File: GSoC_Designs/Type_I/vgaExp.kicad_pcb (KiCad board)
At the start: 2 copper layers, 80 x 60.1 mm, 70 parts, among them J1 DE-15, J2 DE-15, J3 VHDCI, P1 50R, P2 50R, P3 50R, P4 50R, P5 CONN_1, P6 CONN_1, U1 ADP3303-3V3, U2 ADP3334, U3 AD9984, U4 ADP3334

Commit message: PCB Routing
70% tracks routed. Fine tuning remaining
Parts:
- removed C10, C13, C7: 47nf, SM0805
- removed C11: 1nf, SM0805
- removed FB1, FB2, FB3: FILTER, SM0805
- removed P1, P2, P3, P4: 50R, R50x8
- removed R19, R20, R21, R22: 50R, SM0805
- added P7: CONN_6, PIN_ARRAY-6X1, F.Cu at (148.0, 92.5)
- added R23: 2.2K, SM0805, F.Cu at (128.6, 107.3)
- added R24: 4.7K, SM0805, F.Cu at (126.9, 102.8)
- added R25: 4.7K, SM0805, F.Cu at (142.1, 55.8)
- added R26: 4.7K, SM0805, F.Cu at (142.2, 53.7)
- added R27: 4.7K, SM0805, F.Cu at (126.9, 99.9)
- added TP1: TESTPOINT, PIN_ARRAY_1, F.Cu at (153.0, 64.4)
- added TP10: TESTPOINT, PIN_ARRAY_1, F.Cu at (133.4, 51.2)
- added TP11: TESTPOINT, PIN_ARRAY_1, F.Cu at (130.9, 97.5)
- added TP12: TESTPOINT, PIN_ARRAY_1, F.Cu at (95.2, 52.0)
- added TP13: TESTPOINT, PIN_ARRAY_1, F.Cu at (96.6, 60.7)
- added TP2: TESTPOINT, PIN_ARRAY_1, F.Cu at (153.0, 67.0)
- added TP3: TESTPOINT, PIN_ARRAY_1, F.Cu at (126.8, 67.8)
- added TP4: TESTPOINT, PIN_ARRAY_1, F.Cu at (134.7, 67.7)
- added TP5: TESTPOINT, PIN_ARRAY_1, F.Cu at (132.1, 67.7)
- added TP6: TESTPOINT, PIN_ARRAY_1, F.Cu at (129.5, 67.8)
- added TP7: TESTPOINT, PIN_ARRAY_1, F.Cu at (107.3, 91.3)
- added TP8: TESTPOINT, PIN_ARRAY_1, F.Cu at (104.7, 91.3)
- added TP9: TESTPOINT, PIN_ARRAY_1, F.Cu at (115.3, 52.0)
- added U5: 24AA014, -SOIC8, F.Cu at (107.3, 97.1)
- added U6: TCA9617A, SSOP8, F.Cu at (142.6, 60.4)
- added U7: TCA9617A, SSOP8, F.Cu at (130.9, 103.0)
- C17, C18, C19, C2, C21, C22, C23, C24, C25, C3, C4, C5: footprint SM0603 -> SM0805
- Cp1: footprint -PANASONIC_D -> -PANASONIC_D_CorrectedPadNumbers
- Cp2, Cp3, Cp5, Cp6: footprint -PANASONIC_E -> -PANASONIC_E_CorrectedPad
- Cp4: footprint -PANASONIC_C -> -PANASONIC_C_correctedPad
- FB4, FB5, FB6: moved to F.Cu
- R1, R3, R5: value 75R -> 2.2K
- moved R3 29.5 mm to (133.3, 107.4)
- moved R5 19.1 mm to (141.2, 64.9)
- moved R14 7.52 mm to (121.7, 107.7)
- moved R1 6.96 mm to (142.8, 67.3)
- turned FB6 to 180 degrees
- turned FB5 to 180 degrees
- turned FB4 to 180 degrees
- turned C12 to 180 degrees
- turned C6 to 180 degrees
- turned C8 to 180 degrees
- turned C9 to 180 degrees
- turned Cp6 to 90 degrees
- turned R13 to 270 degrees
- turned R18 to 0 degrees
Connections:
- C15 pad 1: /PVD -> /PowerSupply/PVD
- C15 pad 2: N-00000138 -> N-000001
- C16 pad 1: /PVD -> /PowerSupply/PVD
- C16 pad 2: N-000001 -> N-000005
- C17 pad 2: /PowerSupply/GND -> /I2C/DDC Section/GND
- C18 pad 2: /PowerSupply/GND -> /I2C/DDC Section/GND
- C19 pad 2: /PowerSupply/GND -> /I2C/DDC Section/GND
- C2 pad 1: /PowerSupply/OVDD -> /I2C/DDC Section/OVDD
- C2 pad 2: /PowerSupply/GND -> /I2C/DDC Section/GND
- C21 pad 2: /PowerSupply/GND -> /I2C/DDC Section/GND
- C22 pad 2: /PowerSupply/GND -> /I2C/DDC Section/GND
- C23 pad 2: /PowerSupply/GND -> /I2C/DDC Section/GND
- C24 pad 2: /PowerSupply/GND -> /I2C/DDC Section/GND
- C25 pad 2: /PowerSupply/GND -> /I2C/DDC Section/GND
- C3 pad 1: /PowerSupply/OVDD -> /I2C/DDC Section/OVDD
- C3 pad 2: /PowerSupply/GND -> /I2C/DDC Section/GND
- C4 pad 1: /PowerSupply/OVDD -> /I2C/DDC Section/OVDD
- C4 pad 2: /PowerSupply/GND -> /I2C/DDC Section/GND
- C5 pad 1: /PowerSupply/OVDD -> /I2C/DDC Section/OVDD
- C5 pad 2: /PowerSupply/GND -> /I2C/DDC Section/GND
- FB4 pad 1: N-0000037 -> /B
- FB5 pad 1: N-0000068 -> /G
- FB6 pad 1: N-0000072 -> /R
- J1 pad 1: N-0000071 -> /R
- J1 pad 10: (no net) -> /I2C/DDC Section/GND
- J1 pad 12: (no net) -> /I2C/DDC Section/SDA_VGA_TX
- J1 pad 13: (no net) -> /HSYNC0
- J1 pad 14: (no net) -> /VSYNC0
- J1 pad 15: (no net) -> /I2C/DDC Section/SCL_VGA_TX
- J1 pad 2: N-0000070 -> /G
- J1 pad 3: N-0000069 -> /B
- J1 pad 4: /GND -> (no net)
- J1 pad 5: /GND -> /I2C/DDC Section/GND
- J1 pad 6: /GND -> /I2C/DDC Section/GND
- J1 pad 7: /GND -> /I2C/DDC Section/GND
- J1 pad 8: /GND -> /I2C/DDC Section/GND
- J1 pad 9: /GND -> (no net)
- J2 pad 1: N-0000072 -> /R
- J2 pad 10: (no net) -> /I2C/DDC Section/GND
- J2 pad 12: (no net) -> /I2C/DDC Section/SDA_VGA_RX
- J2 pad 13: (no net) -> /HSYNC0
- J2 pad 14: (no net) -> /VSYNC0
- J2 pad 15: (no net) -> /I2C/DDC Section/SCL_VGA_RX
- J2 pad 2: N-0000068 -> /G
- J2 pad 3: N-0000037 -> /B
- J2 pad 4: /GND -> (no net)
- J2 pad 5: /GND -> /I2C/DDC Section/GND
- J2 pad 6: /GND -> /I2C/DDC Section/GND
- J2 pad 7: /GND -> /I2C/DDC Section/GND
- J2 pad 8: /GND -> /I2C/DDC Section/GND
- J2 pad 9: /GND -> (no net)
- J3 pad 11: /GND -> /I2C/DDC Section/GND
- J3 pad 14: /GND -> /I2C/DDC Section/GND
- J3 pad 17: /VCC -> /I2C/DDC Section/VCC
- J3 pad 18: /VCC -> /I2C/DDC Section/VCC
- J3 pad 2: /GND -> /I2C/DDC Section/GND
- J3 pad 21: /GND -> /I2C/DDC Section/GND
- J3 pad 24: /GND -> /I2C/DDC Section/GND
- J3 pad 27: /GND -> /I2C/DDC Section/GND
- J3 pad 30: /GND -> /I2C/DDC Section/GND
- J3 pad 33: /GND -> /I2C/DDC Section/GND
- J3 pad 34: (no net) -> /I2C/DDC Section/SDA_INT
- J3 pad 35: /OE_Field -> /I2C/DDC Section/SCL_VGA_RX_BUF
- J3 pad 36: N-0000067 -> /I2C/DDC Section/GND
- J3 pad 37: /PWRDWN -> /I2C/DDC Section/SDA_VGA_RX_BUF
- J3 pad 39: N-0000067 -> /I2C/DDC Section/GND
- J3 pad 42: N-0000067 -> /I2C/DDC Section/GND
- J3 pad 45: N-0000067 -> /I2C/DDC Section/GND
- J3 pad 48: N-0000067 -> /I2C/DDC Section/GND
- J3 pad 5: /GND -> /I2C/DDC Section/GND
- J3 pad 51: /VCC -> /I2C/DDC Section/VCC
- J3 pad 52: /VCC -> /I2C/DDC Section/VCC
- J3 pad 55: N-0000067 -> /I2C/DDC Section/GND
- J3 pad 58: N-0000067 -> /I2C/DDC Section/GND
- J3 pad 61: N-0000067 -> /I2C/DDC Section/GND
- J3 pad 64: N-0000067 -> /I2C/DDC Section/GND
- J3 pad 65: /CLAMP -> /I2C/DDC Section/SCL_VGA_TX_BUF
- J3 pad 66: /COST -> /I2C/DDC Section/SDA_VGA_TX_BUF
- J3 pad 67: N-0000067 -> /I2C/DDC Section/GND
- J3 pad 68: (no net) -> /I2C/DDC Section/SCL_INT
- J3 pad 8: /GND -> /I2C/DDC Section/GND
- P5 pad 1: (no net) -> /I2C/DDC Section/GND
- P6 pad 1: (no net) -> /I2C/DDC Section/VCC
- R1 pad 1: N-0000078 -> /I2C/DDC Section/OVDD
- R1 pad 2: N-0000054 -> /I2C/DDC Section/SDA_VGA_RX_BUF
- R10 pad 1: (no net) -> /I2C/DDC Section/GND
- R11 pad 1: /GND -> /I2C/DDC Section/GND
- R12 pad 1: /GND -> /I2C/DDC Section/GND
- R14 pad 1: /PowerSupply/GND -> /I2C/DDC Section/GND
- R15 pad 1: N-000005 -> /I2C/DDC Section/SCL_INT
- R15 pad 2: /OVDD -> /I2C/DDC Section/OVDD
- R16 pad 1: N-000006 (its old number) -> /I2C/DDC Section/SDA_INT
- R16 pad 2: /OVDD -> /I2C/DDC Section/OVDD
- R18 pad 1: /PowerSupply/GND -> /I2C/DDC Section/GND
- R2 pad 2: N-0000077 -> /I2C/DDC Section/GND
- R3 pad 1: N-0000078 -> /I2C/DDC Section/OVDD
- R3 pad 2: N-0000056 -> /I2C/DDC Section/SDA_VGA_TX_BUF
- R4 pad 2: N-0000077 -> /I2C/DDC Section/GND
- R5 pad 1: N-0000078 -> /I2C/DDC Section/OVDD
- R5 pad 2: N-0000055 -> /I2C/DDC Section/SCL_VGA_RX_BUF
- R6 pad 2: N-0000077 -> /I2C/DDC Section/GND
- R7 pad 1: (no net) -> /I2C/DDC Section/GND
- R8 pad 1: N-00000138 -> N-000005
- R9 pad 1: (no net) -> /I2C/DDC Section/OVDD
- U1 pad 1: /PowerSupply/OVDD -> /I2C/DDC Section/OVDD
- U1 pad 2: /PowerSupply/OVDD -> /I2C/DDC Section/OVDD
- U1 pad 4: /PowerSupply/GND -> /I2C/DDC Section/GND
- U1 pad 5: /PowerSupply/VCC -> /I2C/DDC Section/VCC
- U1 pad 7: /PowerSupply/VCC -> /I2C/DDC Section/VCC
- U1 pad 8: /PowerSupply/VCC -> /I2C/DDC Section/VCC
- U2 pad 1: /PowerSupply/GND -> /I2C/DDC Section/GND
- U2 pad 2: /PowerSupply/GND -> /I2C/DDC Section/GND
- U2 pad 3: /PowerSupply/VCC -> /I2C/DDC Section/VCC
- U2 pad 4: /PowerSupply/VCC -> /I2C/DDC Section/VCC
- U3 pad 1: /VD -> /PowerSupply/VD
- U3 pad 10: N-0000082 -> (no net)
- U3 pad 11: /GND -> /I2C/DDC Section/GND
- U3 pad 12: N-0000083 -> (no net)
- U3 pad 13: /VD -> /PowerSupply/VD
- U3 pad 15: /GND -> /I2C/DDC Section/GND
- U3 pad 16: N-0000085 (its old number) -> (no net)
- U3 pad 21: N-000007 (its old number) -> /OE_Field
- U3 pad 22: N-0000010 (its old number) -> /VSOUT
- U3 pad 23: N-000009 (its old number) -> /HSOUT
- U3 pad 24: N-000008 (its old number) -> /SOGOUT
- U3 pad 25: N-0000033 -> /DATACK
- U3 pad 26: (no net) -> /I2C/DDC Section/OVDD
- U3 pad 27: (no net) -> /I2C/DDC Section/GND
- U3 pad 28: N-0000032 -> /R9
- U3 pad 29: N-0000031 -> /R8
- U3 pad 3: /GND -> /I2C/DDC Section/GND
- U3 pad 30: N-0000030 -> /R7
- U3 pad 31: N-0000029 -> /R6
- U3 pad 32: N-0000028 -> /R5
- U3 pad 33: N-0000027 -> /R4
- U3 pad 34: N-0000026 -> /R3
- U3 pad 35: N-0000025 -> /R2
- U3 pad 36: N-0000015 -> /R1
- U3 pad 37: N-0000024 -> /R0
- U3 pad 38: (no net) -> /I2C/DDC Section/OVDD
- U3 pad 39: N-0000076 -> /I2C/DDC Section/GND
- U3 pad 4: N-0000079 -> (no net)
- U3 pad 40: N-0000076 -> /I2C/DDC Section/GND
- U3 pad 41: /VD -> /PowerSupply/VD
- U3 pad 42: N-00000111 -> /G9
- U3 pad 43: N-00000112 -> /G8
- U3 pad 44: N-00000113 -> /G7
- U3 pad 45: N-00000131 -> /G6
- U3 pad 46: N-00000130 -> /G5
- U3 pad 47: N-00000134 -> /G4
- U3 pad 48: N-00000119 -> /G3
- U3 pad 49: N-00000122 -> /G2
- U3 pad 5: /VD -> /PowerSupply/VD
- U3 pad 50: N-00000115 -> /G1
- U3 pad 51: N-00000117 -> /G0
- U3 pad 52: (no net) -> /I2C/DDC Section/OVDD
- U3 pad 53: (no net) -> /I2C/DDC Section/GND
- U3 pad 54: N-00000114 -> /B9
- U3 pad 55: N-00000132 -> /B8
- U3 pad 56: N-00000133 -> /B7
- U3 pad 57: N-00000135 -> /B6
- U3 pad 58: N-00000120 -> /B5
- U3 pad 59: N-00000118 -> /B4
- U3 pad 60: N-00000116 -> /B3
- U3 pad 61: N-000003 -> /B2
- U3 pad 62: N-000002 -> /B1
- U3 pad 63: N-000004 -> /B0
- U3 pad 64: (no net) -> /I2C/DDC Section/OVDD
- U3 pad 65: (no net) -> /I2C/DDC Section/GND
- U3 pad 66: N-000006 (its old number) -> /I2C/DDC Section/SDA_INT
- U3 pad 67: N-000005 -> /I2C/DDC Section/SCL_INT
- U3 pad 68: (no net) -> /I2C/DDC Section/GND
- U3 pad 69: (no net) -> /I2C/DDC Section/GND
- U3 pad 7: /GND -> /I2C/DDC Section/GND
- U3 pad 70: (no net) -> /HSYNC0
- U3 pad 71: (no net) -> /VSYNC0
- U3 pad 74: /PVD -> /PowerSupply/PVD
- U3 pad 75: /GND -> /I2C/DDC Section/GND
- U3 pad 76: /PVD -> /PowerSupply/PVD
- U3 pad 77: /GND -> /I2C/DDC Section/GND
- U3 pad 78: N-00000138 -> N-000001
- U3 pad 79: /PVD -> /PowerSupply/PVD
- U3 pad 80: /GND -> /I2C/DDC Section/GND
- U3 pad 9: /VD -> /PowerSupply/VD
- U4 pad 1: /PowerSupply/GND -> /I2C/DDC Section/GND
- U4 pad 2: /PowerSupply/GND -> /I2C/DDC Section/GND
- U4 pad 3: /PowerSupply/VCC -> /I2C/DDC Section/VCC
- U4 pad 4: /PowerSupply/VCC -> /I2C/DDC Section/VCC
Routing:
- net /I2C/DDC Section/VCC: track 0.00 -> 132.5 mm, vias 0 -> 1
- net /HSYNC0: track 0.00 -> 80.2 mm
- net /VSYNC0: track 0.00 -> 77.3 mm
- net /I2C/DDC Section/SDA_VGA_RX_BUF: track 0.00 -> 65.9 mm
- net /I2C/DDC Section/SCL_VGA_RX_BUF: track 0.00 -> 63.7 mm
- net /I2C/DDC Section/SDA_VGA_TX_BUF: track 0.00 -> 56.7 mm, vias 0 -> 1
- net /I2C/DDC Section/SCL_VGA_TX_BUF: track 0.00 -> 51.2 mm, vias 0 -> 1
- net /B: track 0.00 -> 47.9 mm
- net /I2C/DDC Section/OVDD: track 0.00 -> 46.5 mm
- net /VSOUT: track 0.00 -> 44.3 mm, vias 0 -> 1
- net /G: track 0.00 -> 40.3 mm
- net /R: track 0.00 -> 37.1 mm
- net /HSOUT: track 0.00 -> 36.8 mm
- net /DATACK: track 0.00 -> 36.7 mm, vias 0 -> 1
- net /R9: track 0.00 -> 35.6 mm
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- added copper zone on B.Cu, net /I2C/DDC Section/GND
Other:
- net class Default: clearance 0.254 -> 0.125; trace_width 0.254 -> 0.125; via_dia 0.889 -> 0.45; via_drill 0.635 -> 0.3
- rule trace_clearance: 0.254 -> 0.125
- rule trace_min: 0.254 -> 0.125
- rule via_min_drill: 0.508 -> 0.3
- rule via_min_size: 0.889 -> 0.45

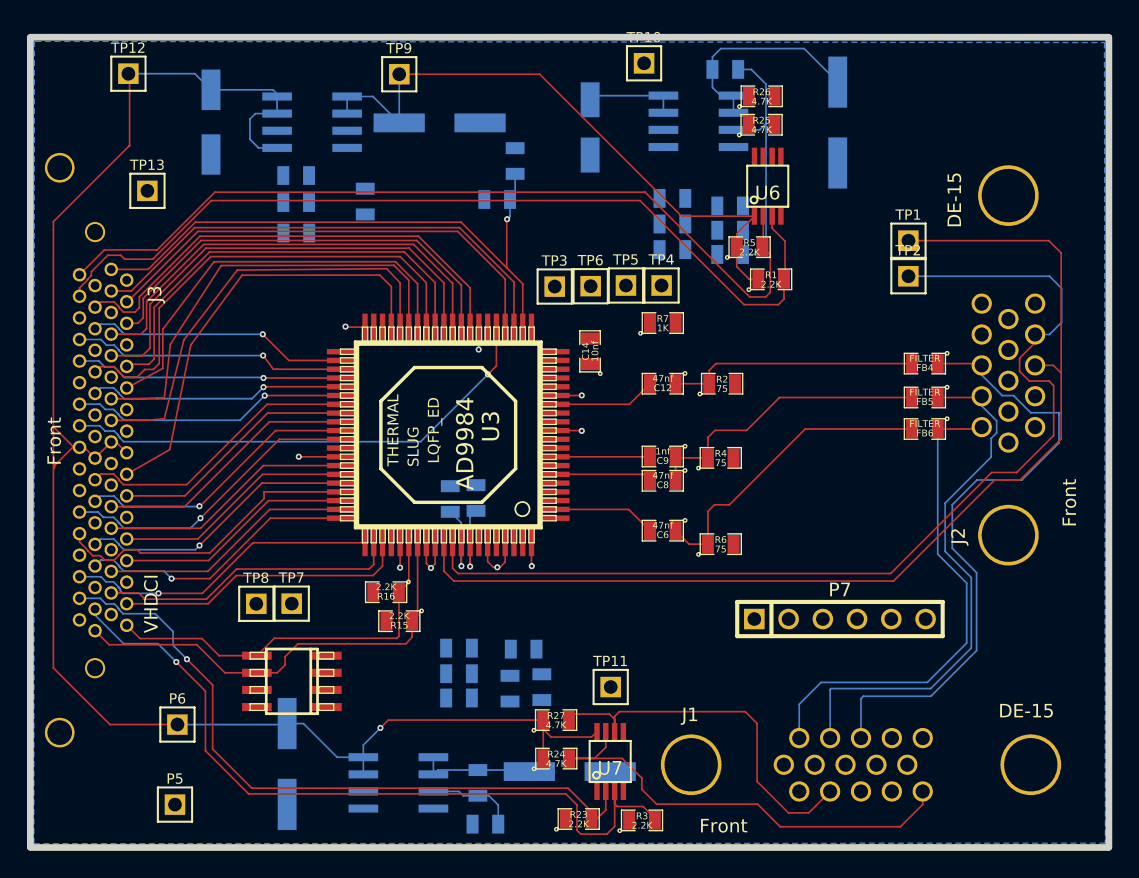
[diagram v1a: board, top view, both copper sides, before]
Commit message: All tracks routed. Optimizations and dine tuning remain
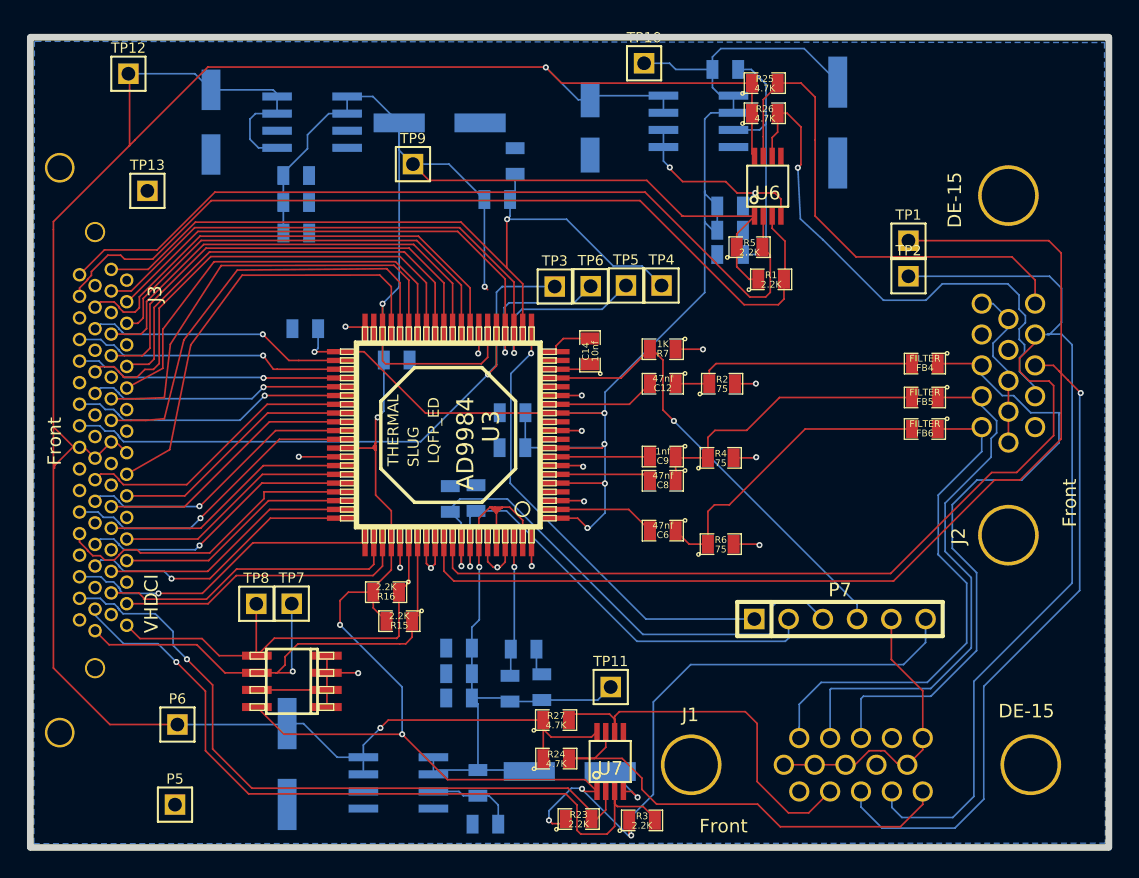
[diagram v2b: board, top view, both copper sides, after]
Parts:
- moved C21 27.9 mm to (108.3, 70.9)
- moved C22 20.4 mm to (123.7, 79.7)
- moved C23 19.8 mm to (123.7, 77.2)
- moved C5 12.0 mm to (115.1, 73.2), turned to 0 degrees
- moved TP9 6.74 mm to (116.3, 58.7)
- moved R25 3.10 mm to (142.4, 52.7)
- moved R7 1.94 mm to (134.8, 72.4), turned to 180 degrees
- moved R26 1.28 mm to (142.4, 54.9)
- turned R8 to 180 degrees
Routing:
- net /I2C/DDC Section/OVDD: track 46.5 -> 215.0 mm, vias 0 -> 8
- net /PowerSupply/VD: track 15.9 -> 111.9 mm, vias 0 -> 5
- net /I2C/DDC Section/GND: track 22.8 -> 99.7 mm, vias 9 -> 19
- net /I2C/DDC Section/VCC: track 132.5 -> 191.4 mm, vias 1 -> 2
- net /HSYNC0: track 80.2 -> 127.4 mm, vias 0 -> 1
- net /VSYNC0: track 77.3 -> 124.2 mm
- net /PowerSupply/PVD: track 8.56 -> 49.4 mm, vias 0 -> 1
- net /I2C/DDC Section/SDA_VGA_RX: track 0.00 -> 40.6 mm, vias 0 -> 1
- net /I2C/DDC Section/SCL_VGA_RX: track 0.00 -> 37.9 mm
- net /COST: track 6.10 -> 41.1 mm
- net /OE_Field: track 0.00 -> 34.6 mm, vias 0 -> 1
- net /PWRDWN: track 0.00 -> 34.3 mm, vias 0 -> 1
- net /CLAMP: track 6.07 -> 34.8 mm
- net /HSOUT: track 36.8 -> 50.7 mm, vias 0 -> 1
- net /VSOUT: track 44.3 -> 57.8 mm
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
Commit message: All Tracks routed. Tweaks. Ready for review
All Tracks routed. Tweaks. Ready for review. Some minor changes and
tweaks may be done before sending for Fab
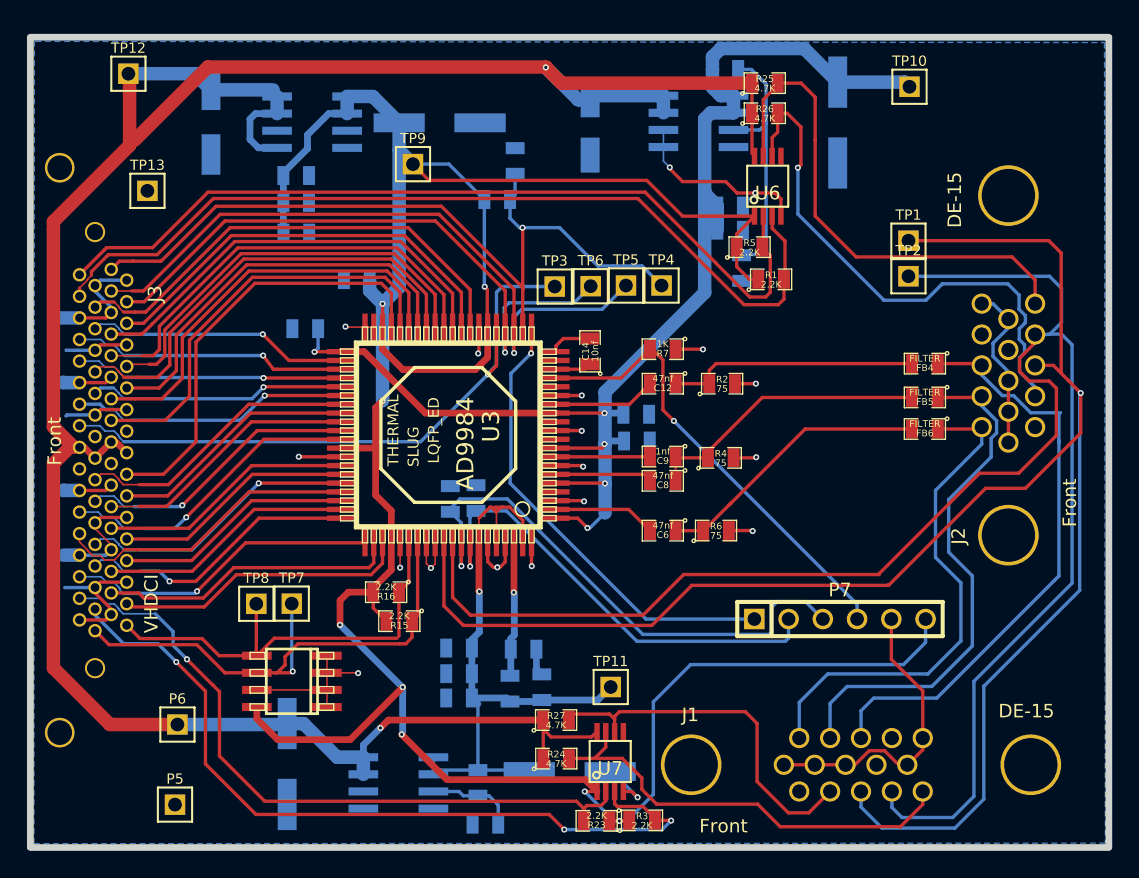
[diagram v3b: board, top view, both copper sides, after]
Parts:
- added ?: , OSHW-logo_silkscreen-back_10mm, B.Cu at (140.4, 83.0)
- moved TP10 19.8 mm to (153.1, 53.0)
- moved C22 9.25 mm to (132.9, 79.2), turned to 0 degrees
- moved C23 9.17 mm to (132.8, 77.3), turned to 0 degrees
- moved C5 6.65 mm to (112.1, 67.3), turned to 180 degrees
- moved R23 1.34 mm to (129.9, 107.4), turned to 180 degrees
- moved R18 1.32 mm to (140.7, 66.4), turned to 90 degrees
- moved R6 1.07 mm to (138.8, 85.9)
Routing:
- net /I2C/DDC Section/GND: track 99.7 -> 144.2 mm
- net /PowerSupply/VD: track 111.9 -> 100.5 mm
- net /VSYNC0: track 124.2 -> 128.3 mm
- net /HSYNC0: track 127.4 -> 131.4 mm
- net /B: track 47.9 -> 44.4 mm
- net /I2C/DDC Section/VCC: track 191.4 -> 188.5 mm
- net /I2C/DDC Section/SDA_VGA_TX_BUF: track 56.7 -> 58.9 mm, vias 1 -> 3
- net /B9: track 18.9 -> 21.1 mm
- net N-0000061: track 22.9 -> 21.0 mm
- net /R2: track 32.7 -> 31.0 mm
- net /R5: track 32.9 -> 31.1 mm
- net /R4: track 35.3 -> 33.7 mm
- net /VSOUT: track 57.8 -> 59.3 mm
- net /R7: track 33.7 -> 32.3 mm
- net /R6: track 34.2 -> 32.8 mm
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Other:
- board text added: "vMod-VGA"
